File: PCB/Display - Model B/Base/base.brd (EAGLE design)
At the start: 121.9 x 17.8 mm, 36 parts, among them J1 SNG-2MM-HEADER-07-V, Q1 MMBT3904, Q2 MMBT3904, Q3 MMBT3904, Q4 MMBT3904, U1 PCA9634PW, U2 TSL2561FN, X1 CLOCK_LED_SEGMENT, X2 CLOCK_LED_SEGMENT, X3 CLOCK_LED_SEGMENT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

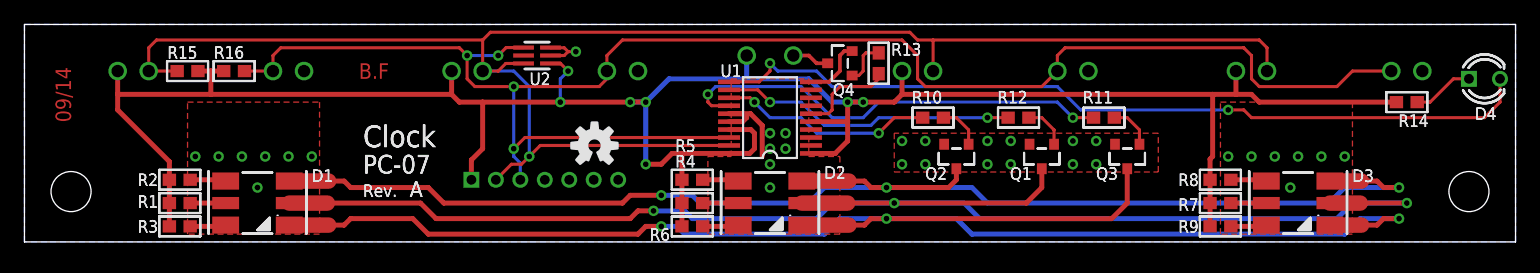
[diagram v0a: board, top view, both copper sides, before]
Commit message: Added decoupling caps
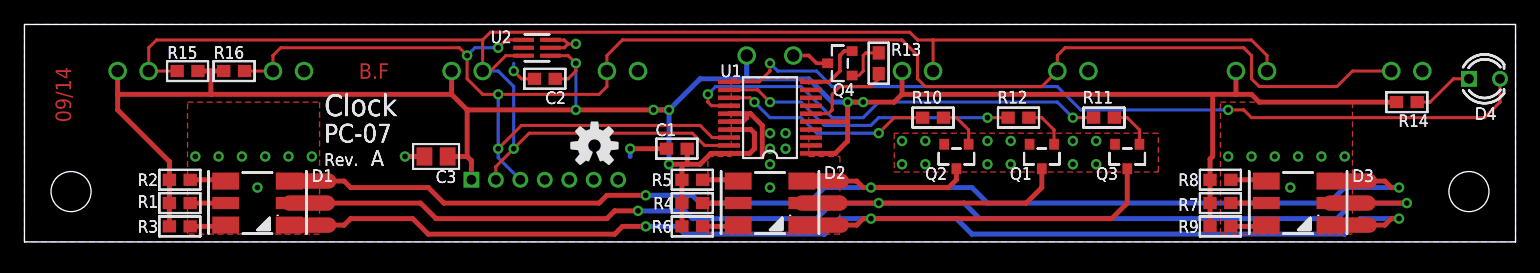
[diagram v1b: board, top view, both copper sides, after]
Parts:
- added C1, C2: 100nF, Passive:SMD_0603
- added C3: N/A, Passive:SMD_0805
- moved U$4 4.07 mm to (29.6, 8.76)
- moved U2 0.63 mm to (41.9, 15.9)
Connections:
- net 3.3V: now also C1.1, C2.2, C3.1
- net GND: now also C1.2, C2.1, C3.2
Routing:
- net GND: track 17.7 -> 25.5 mm, vias 33 -> 36
- net 3.3V: track 191.2 -> 194.5 mm
- net SCL: track 138.8 -> 142.0 mm
- net SDA: track 137.6 -> 137.0 mm
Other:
- board text added: "C1"
- board text added: "C2"
- board text added: "C3"
